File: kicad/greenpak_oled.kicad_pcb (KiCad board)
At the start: 2 copper layers, 35.6 x 35.6 mm, 21 parts, among them J1 Conn_01x05_Pin, J2 Conn_01x03_Socket, U1 SLG46826G, U2 OLED-128O064D

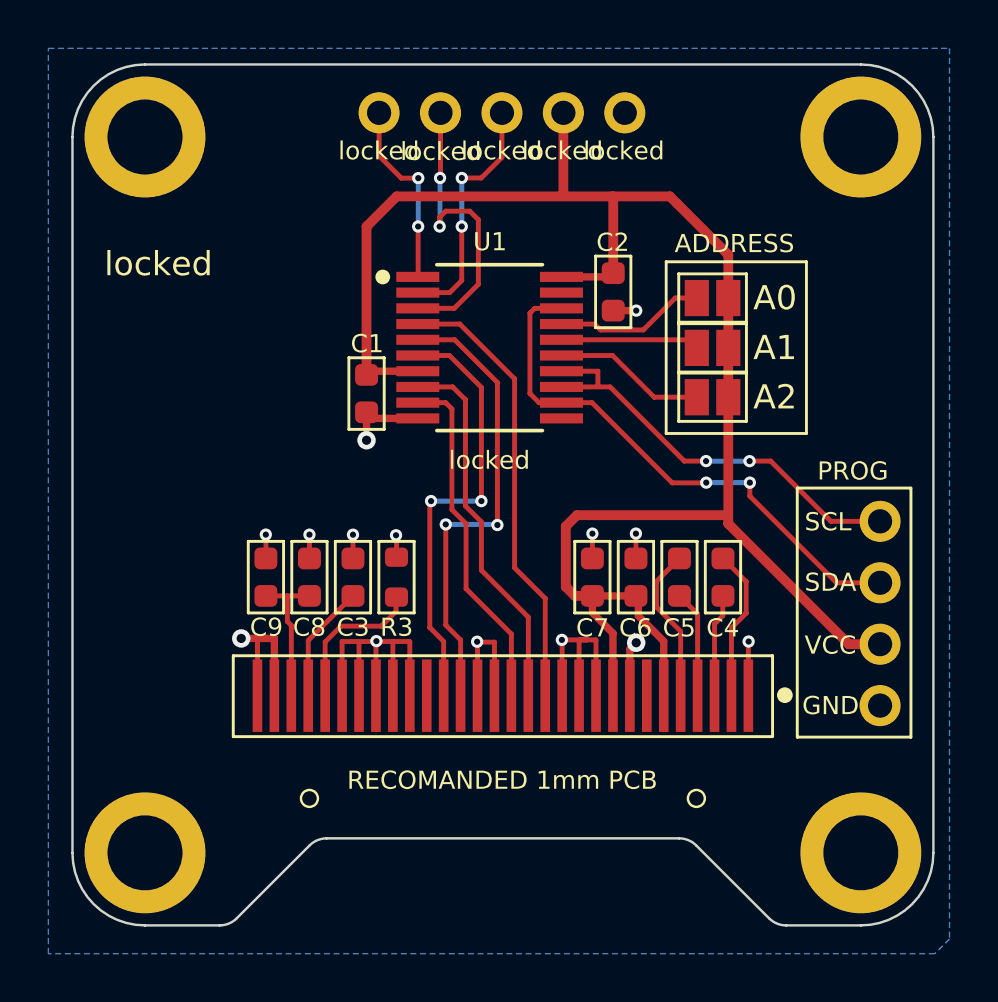
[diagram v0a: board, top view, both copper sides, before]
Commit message: Renamed left over addressable_oled to greenpak_oled.
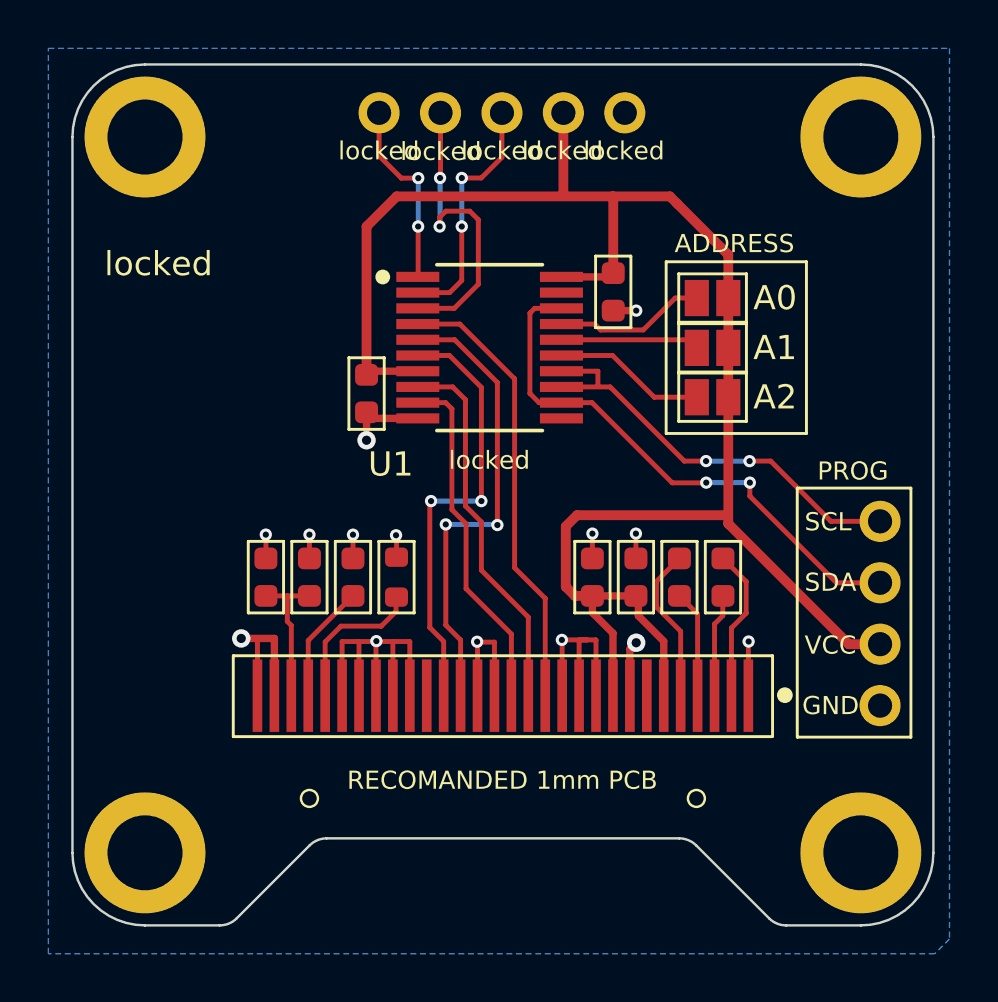
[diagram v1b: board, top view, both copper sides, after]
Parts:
- C1, C2, C3, C4, C5, C6, C7, C8, C9: footprint addressable_oled:C_0603_1608Metric -> greenpak_oled:C_0603_1608Metric
- H1, H2, H3, H4: footprint addressable_oled:MountingHole -> greenpak_oled:MountingHole
- J1: footprint addressable_oled:PinHeader_1x05_P2.54mm_Vertical -> greenpak_oled:PinHeader_1x05_P2.54mm_Vertical
- J2: footprint addressable_oled:PinHeader_1x04_P2.54mm_Vertical -> greenpak_oled:PinHeader_1x04_P2.54mm_Vertical
- JP1, JP2, JP4: footprint addressable_oled:SolderJumper-2_P1.3mm_Open_Pad1.0x1.5mm -> greenpak_oled:SolderJumper-2_P1.3mm_Open_Pad1.0x1.5mm
- R3: footprint addressable_oled:R_0603_1608Metric -> greenpak_oled:R_0603_1608Metric
- U1: footprint addressable_oled:TSSOP20_MO-220_WECE_REN -> greenpak_oled:TSSOP20_MO-220_WECE_REN
- U2: footprint addressable_oled:OLED-128O064D -> greenpak_oled:OLED-128O064D

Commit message: Final touched. Regenerated gerbers.
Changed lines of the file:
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@@
     (property "ki_keywords" "SLG46826G")
     (attr smd)
-    (fp_text reference "U1" (at -4.0894 4.826 unlocked) (layer "F.SilkS")
+    (fp_text reference "U1" (at -4.0894 4.826 unlocked) (layer "F.SilkS") hide
         (effects (font (size 1 1) (thickness 0.15)))
     )
@@
     (effects (font (size 0.75 0.75) (thickness 0.1)))
   )
-  (gr_text locked "ADDRESSABLE\nSPI OLED\nSSD1306\n3.3V\n\nADDR 0-7\nJMPR=1\n\nV 0.1" (at -16.4846 -10.1346) (layer "F.SilkS")
+  (gr_text locked "GREENPAK\nADDRESSABLE\nSPI OLED\nSSD1306\n3.3V\nADDR 0-7\nJMPR=1\nV 0.1" (at -16.4846 -10.1346) (layer "F.SilkS")
     (effects (font (size 1 1) (thickness 0.15)) (justify left top))
   )

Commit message: Fixed a typo in the silkscreen
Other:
- board text added: "RECOMMENDED 1mm PCB"
- board text removed: "RECOMANDED 1mm PCB"
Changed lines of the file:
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@@
     (effects (font (size 1.5 1.5) (thickness 0.2)) (justify mirror))
   )
-  (gr_text "RECOMANDED 1mm PCB" (at -0.0254 12.2428) (layer "F.SilkS")
+  (gr_text "RECOMMENDED 1mm PCB" (at -0.0254 12.2428) (layer "F.SilkS")
     (effects (font (size 0.75 0.75) (thickness 0.1)) (justify bottom))
   )

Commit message: Changed programming pads to pogo socket.
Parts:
- removed J2: Conn_01x03_Socket, greenpak_oled:PinHeader_1x04_P2.54mm_Vertical
- added J3: POGO_SOCKET, greenpak_oled:POGO_SOCKET, F.Cu at (16.0, 2.36)
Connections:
- net /I2C_CLK renamed Net-(J3-SCL)
- net /I2C_DAT renamed Net-(J3-SDA)
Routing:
- net VDD: track 73.4 -> 70.4 mm
- net Net-(J3-SDA): track 22.7 -> 24.0 mm
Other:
- board text removed: "GND"
- board text removed: "SCL"
- board text removed: "SDA"
- board text removed: "VCC"
